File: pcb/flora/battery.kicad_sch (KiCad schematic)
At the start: 38 parts, among them IC3 TP4056X, IC4 FS8205A, IC5 DW01+G, IC6 TPS54302DDCR, IC7 AMS1117-3.3

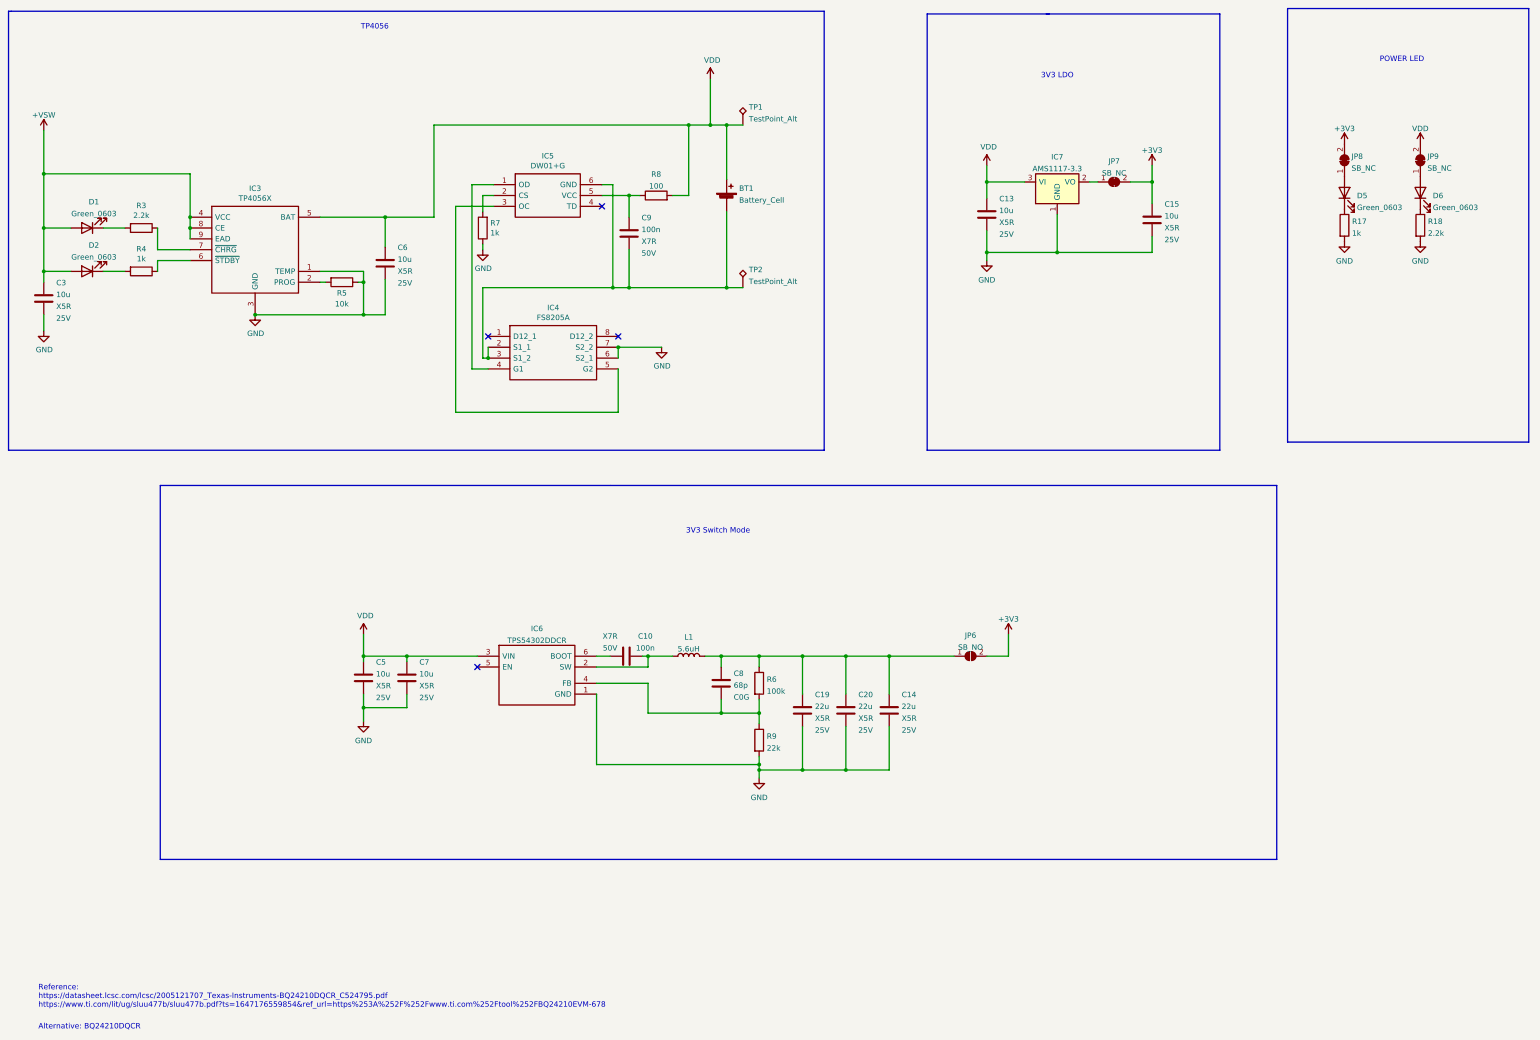
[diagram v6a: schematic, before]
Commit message: Finished schematic for RA-01 design
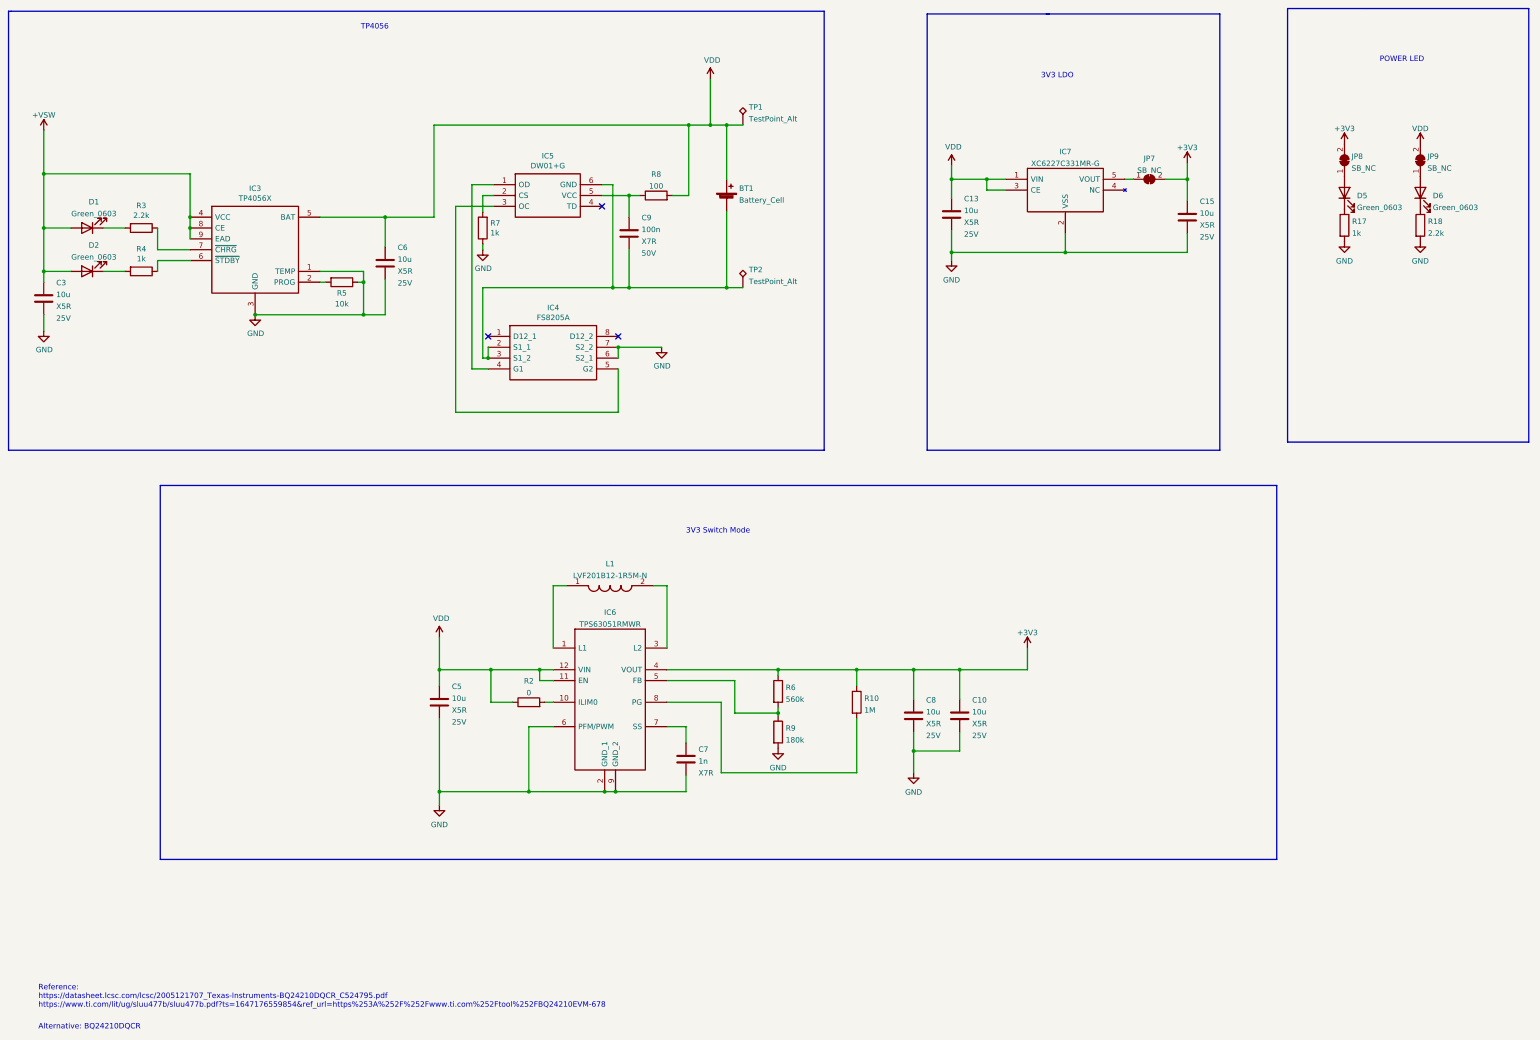
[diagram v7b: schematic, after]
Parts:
- removed C10: 100n, Capacitor_SMD:C_0402_1005Metric, symbol Capacitor_JLC:100n
- removed C14, C19, C20: 22u, Capacitor_SMD:C_0805_2012Metric, symbol Capacitor_JLC:22u
- removed C7: 10u, Capacitor_SMD:C_0805_2012Metric, symbol Capacitor_JLC:10u
- removed C8: 68p, Capacitor_SMD:C_0402_1005Metric, symbol Capacitor_JLC:68p
- removed IC6: TPS54302DDCR, SOT95P280X110-6N, symbol Power-Drivers_JLC:TPS54302DDCR
- removed IC7: AMS1117-3.3, Package_TO_SOT_SMD:SOT-223-3_TabPin2, symbol Power-Drivers_JLC:AMS1117-3.3
- removed JP6: SB_NO, Jumper:SolderJumper-2_P1.3mm_Open_TrianglePad1.0x1.5mm, symbol personal:SB_NO
- removed L1: 5.6uH, SamacSys_Parts:INDPM4040X300N, symbol Inductor_JLC:5.6uH
- removed R6: 100k, Resistor_SMD:R_0402_1005Metric, symbol Resistor_JLC:100k
- removed R9: 22k, Resistor_SMD:R_0402_1005Metric, symbol Resistor_JLC:22k
- added C10, C8: 10u, Capacitor_SMD:C_0805_2012Metric, symbol Capacitor_JLC:10u
- added C7: 1n, Capacitor_SMD:C_0402_1005Metric, symbol Capacitor_JLC:1n
- added IC6: TPS63051RMWR, QFN50P250X250X100-12N-D, symbol Power-Drivers_JLC:TPS63051RMWR
- added IC7: XC6227C331MR-G, SOT95P280X130-5N, symbol Power-Drivers_JLC:XC6227C331MR-G
- added L1: LVF201B12-1R5M-N, LVF201B121R5MN, symbol Inductor_JLC:LVF201B12-1R5M-N
- added R10: 1M, Resistor_SMD:R_0402_1005Metric, symbol Resistor_JLC:1M
- added R2: 0, Resistor_SMD:R_0805_2012Metric_Pad1.20x1.40mm_HandSolder, symbol Resistor_JLC:0
- added R6: 560k, Resistor_SMD:R_0603_1608Metric, symbol Resistor_JLC:560k
- added R9: 180k, Resistor_SMD:R_0402_1005Metric, symbol Resistor_JLC:180k
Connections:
- net +3V3: now also C10.1, C8.1, IC6.4 (VOUT), R10.1, R6.1
- net GND: now also C10.2, C7.2, C8.2, IC6.2 (GND_1), IC6.6 (PFM/PWM), IC6.9 (GND_2), IC7.2 (VSS), R9.2
- net VDD: now also IC6.11 (EN), IC6.12 (VIN), IC7.1 (VIN), IC7.3 (CE), R2.1
- net at JP7.1 (A): now also IC7.5 (VOUT)
- new net: IC6.5 (FB), R6.2, R9.1
- new net: C7.1, IC6.7 (SS)
- new net: IC6.10 (ILIM0), R2.2
- new net: IC6.1 (L1), L1.1
- new net: IC6.3 (L2), L1.2
- new net: IC6.8 (PG), R10.2
- no-connect marks 4 -> 3
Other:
- title: FLORA -> FLORA-RA01H
- moved on the sheet: C13, C15, JP7

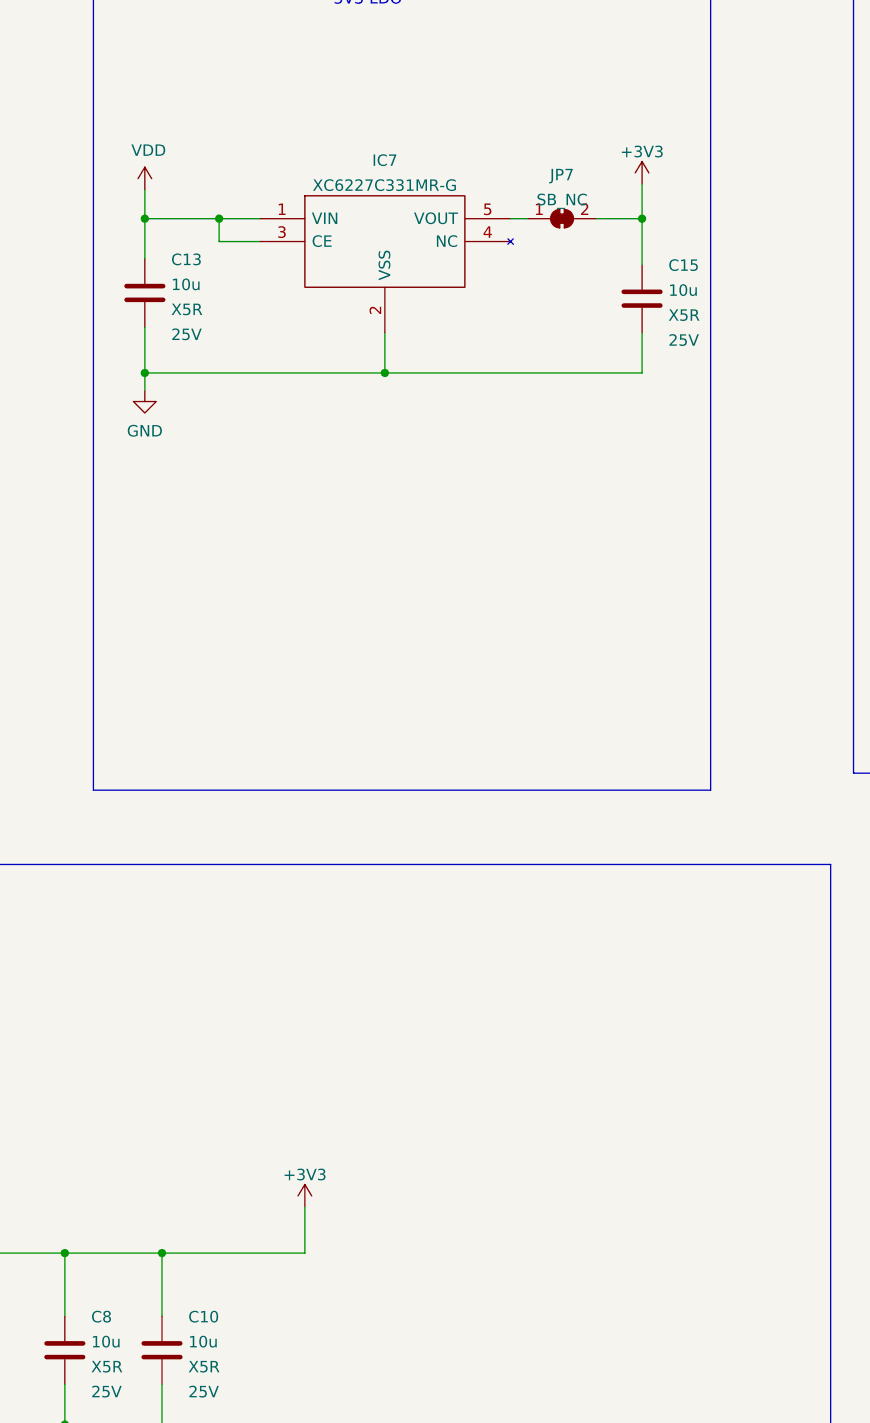
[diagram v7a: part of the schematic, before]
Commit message: base placement completed
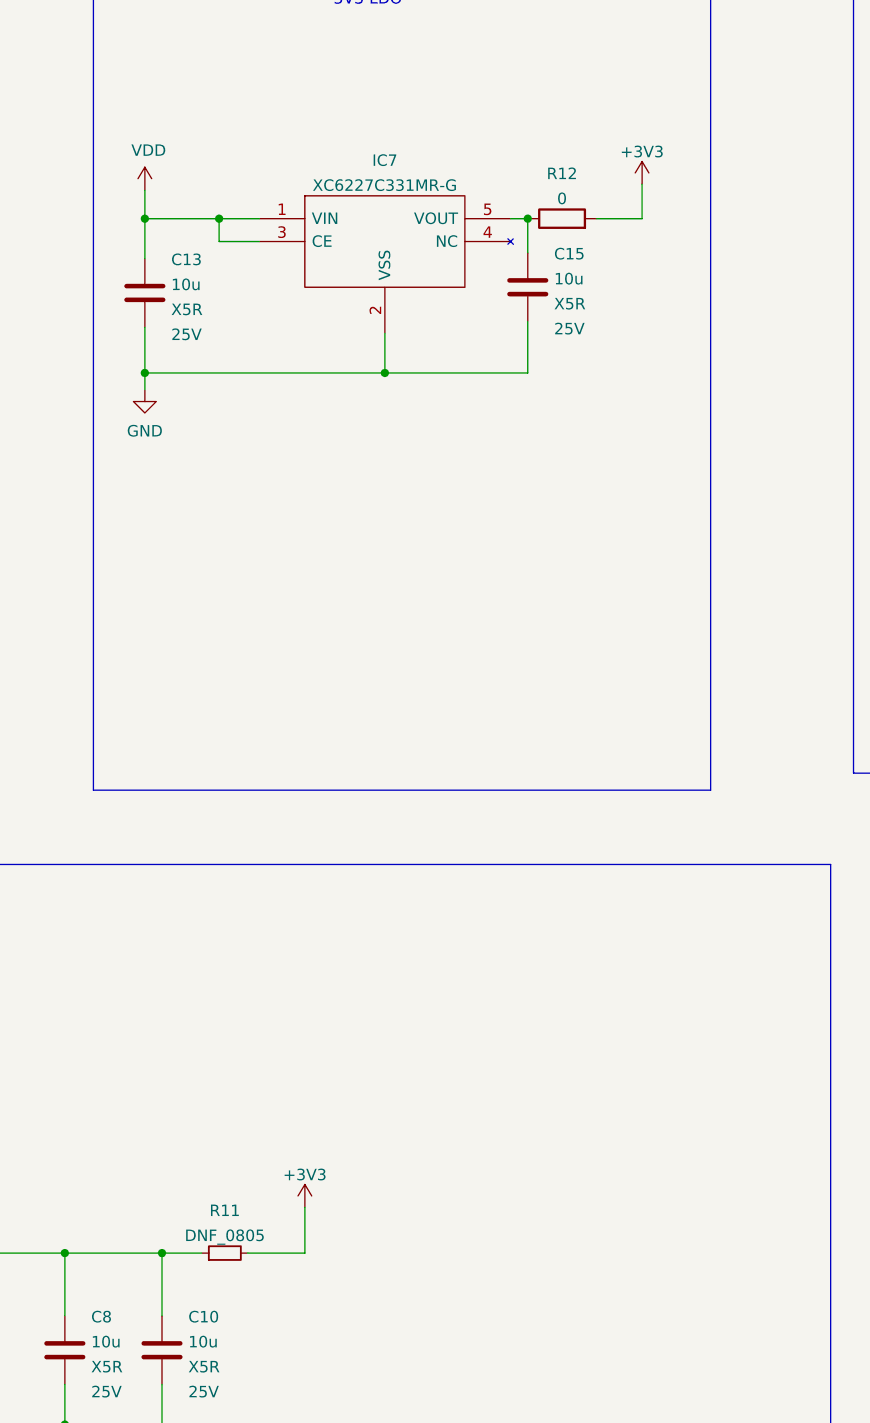
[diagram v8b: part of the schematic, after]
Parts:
- removed JP7: SB_NC, Jumper:SolderJumper-2_P1.3mm_Bridged_Pad1.0x1.5mm, symbol personal:SB_NC
- added R11: DNF_0805, Resistor_SMD:R_0805_2012Metric_Pad1.20x1.40mm_HandSolder, symbol personal:DNF_0805
- added R12: 0, Resistor_SMD:R_0805_2012Metric_Pad1.20x1.40mm_HandSolder, symbol Resistor_JLC:0
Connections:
- net +3V3: now also R11.2, R12.2; no longer C10.1, C15.1, C8.1, IC6.4 (VOUT), R10.1, R6.1
- net at IC7.5 (VOUT): now also C15.1, R12.1
- new net: C10.1, C8.1, IC6.4 (VOUT), R10.1, R11.1, R6.1
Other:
- moved on the sheet: C15
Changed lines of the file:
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@@
   (junction (at 256.54 204.47) (diameter 0) (color 0 0 0 0)
   )
-  (junction (at 320.675 70.485) (diameter 0) (color 0 0 0 0)
-  )
   (junction (at 265.43 87.63) (diameter 0) (color 0 0 0 0)
   )
+  (junction (at 307.975 70.485) (diameter 0) (color 0 0 0 0)
+  )
   (junction (at 127.635 102.235) (diameter 0) (color 0 0 0 0)
   )
@@
   (junction (at 212.725 95.885) (diameter 0) (color 0 0 0 0)
   )
+  (junction (at 157.48 185.42) (diameter 0) (color 0 0 0 0)
+  )
+  (junction (at 208.915 57.785) (diameter 0) (color 0 0 0 0)
+  )
+  (junction (at 102.235 102.235) (diameter 0) (color 0 0 0 0)
+  )
+  (junction (at 273.685 70.485) (diameter 0) (color 0 0 0 0)
+  )
   (junction (at 267.335 185.42) (diameter 0) (color 0 0 0 0)
-  )
-  (junction (at 157.48 185.42) (diameter 0) (color 0 0 0 0)
-  )
-  (junction (at 208.915 57.785) (diameter 0) (color 0 0 0 0)
-  )
-  (junction (at 102.235 102.235) (diameter 0) (color 0 0 0 0)
-  )
-  (junction (at 273.685 70.485) (diameter 0) (color 0 0 0 0)
   )
   (junction (at 86.995 81.915) (diameter 0) (color 0 0 0 0)
@@
     (stroke (width 0) (type default) (color 0 0 0 0))
   )
+  (wire (pts (xy 307.975 81.915) (xy 307.975 87.63))
+    (stroke (width 0) (type default) (color 0 0 0 0))
+  )
   (wire (pts (xy 187.325 109.855) (xy 187.325 112.395))
     (stroke (width 0) (type default) (color 0 0 0 0))
   )
+  (wire (pts (xy 208.915 57.785) (xy 212.725 57.785))
+    (stroke (width 0) (type default) (color 0 0 0 0))
+  )
+  (wire (pts (xy 117.475 94.615) (xy 118.745 94.615))
+    (stroke (width 0) (type default) (color 0 0 0 0))
+  )
   (wire (pts (xy 315.595 70.485) (xy 320.675 70.485))
     (stroke (width 0) (type default) (color 0 0 0 0))
   )
-  (wire (pts (xy 208.915 57.785) (xy 212.725 57.785))
-    (stroke (width 0) (type default) (color 0 0 0 0))
-  )
-  (wire (pts (xy 117.475 94.615) (xy 118.745 94.615))
-    (stroke (width 0) (type default) (color 0 0 0 0))
-  )
   (wire (pts (xy 224.79 194.31) (xy 224.79 195.58))
     (stroke (width 0) (type default) (color 0 0 0 0))
@@
     (stroke (width 0) (type default) (color 0 0 0 0))
   )
-  (wire (pts (xy 320.675 70.485) (xy 320.675 75.565))
-    (stroke (width 0) (type default) (color 0 0 0 0))
-  )
   (wire (pts (xy 265.43 82.55) (xy 265.43 87.63))
     (stroke (width 0) (type default) (color 0 0 0 0))
@@
     (stroke (width 0) (type default) (color 0 0 0 0))
   )
+  (wire (pts (xy 276.86 185.42) (xy 283.21 185.42))
+    (stroke (width 0) (type default) (color 0 0 0 0))
+  )
+  (wire (pts (xy 267.335 185.42) (xy 271.78 185.42))
+    (stroke (width 0) (type default) (color 0 0 0 0))
+  )
   (polyline (pts (xy 80.01 229.87) (xy 80.01 142.24))
     (stroke (width 0) (type default) (color 0 0 0 0))
@@
     (stroke (width 0) (type default) (color 0 0 0 0))
   )
-  (wire (pts (xy 292.1 87.63) (xy 320.675 87.63))
+  (wire (pts (xy 292.1 87.63) (xy 307.975 87.63))
     (stroke (width 0) (type default) (color 0 0 0 0))
   )
@@
     (stroke (width 0) (type default) (color 0 0 0 0))
   )
-  (wire (pts (xy 320.675 87.63) (xy 320.675 83.185))
-    (stroke (width 0) (type default) (color 0 0 0 0))
-  )
   (polyline (pts (xy 259.715 133.985) (xy 259.715 31.75))
     (stroke (width 0) (type default) (color 0 0 0 0))
@@
     (stroke (width 0) (type default) (color 0 0 0 0))
   )
+  (wire (pts (xy 307.975 70.485) (xy 307.975 74.295))
+    (stroke (width 0) (type default) (color 0 0 0 0))
+  )
   (wire (pts (xy 183.515 74.295) (xy 189.865 74.295))
     (stroke (width 0) (type default) (color 0 0 0 0))
@@
   )
   (wire (pts (xy 203.835 57.785) (xy 208.915 57.785))
-    (stroke (width 0) (type default) (color 0 0 0 0))
-  )
-  (wire (pts (xy 267.335 185.42) (xy 283.21 185.42))
     (stroke (width 0) (type default) (color 0 0 0 0))
   )
@@
     (pin "1")
   )
-  (symbol (lib_id "personal:SB_NC") (at 311.785 70.485 0) (unit 1)
-    (in_bom yes) (on_board yes) (fields_autoplaced)
-    (property "Reference" "JP7" (id 0) (at 311.785 65.6295 0))
-    (property "Value" "SB_NC" (id 1) (at 311.785 68.4046 0))
-    (property "Footprint" "Jumper:SolderJumper-2_P1.3mm_Bridged_Pad1.0x1.5mm" (id 2) (at 311.785 70.485 0)
+  (symbol (lib_id "Resistor_JLC:0") (at 311.785 70.485 90) (unit 1)
+    (in_bom yes) (on_board yes) (fields_autoplaced)
+    (property "Reference" "R12" (id 0) (at 311.785 65.5025 90))
+    (property "Value" "0" (id 1) (at 311.785 68.2776 90))
+    (property "Footprint" "Resistor_SMD:R_0805_2012Metric_Pad1.20x1.40mm_HandSolder" (id 2) (at 311.785 72.263 90)
       (effects (font (size 1.27 1.27)) hide)
     )
     (property "Datasheet" "~" (id 3) (at 311.785 70.485 0)
+      (effects (font (size 1.27 1.27)) hide)
+    )
+    (property "LCSC" "C17477" (id 4) (at 311.785 70.485 0)
       (effects (font (size 1.27 1.27)) hide)
     )
@@
     (pin "8")
   )
-  (symbol (lib_id "Capacitor_JLC:10u") (at 320.675 79.375 0) (unit 1)
-    (in_bom yes) (on_board yes) (fields_autoplaced)
-    (property "Reference" "C15" (id 0) (at 323.596 75.6914 0)
-      (effects (font (size 1.27 1.27)) (justify left))
-    )
-    (property "Value" "10u" (id 1) (at 323.596 78.4665 0)
-      (effects (font (size 1.27 1.27)) (justify left))
-    )
-    (property "Footprint" "Capacitor_SMD:C_0805_2012Metric" (id 2) (at 321.6402 83.185 0)
-      (effects (font (size 1.27 1.27)) hide)
-    )
-    (property "Datasheet" "~" (id 3) (at 320.675 79.375 0)
-      (effects (font (size 1.27 1.27)) hide)
-    )
-    (property "Type" "X5R" (id 4) (at 323.596 81.2416 0)
-      (effects (font (size 1.27 1.27)) (justify left))
-    )
-    (property "LCSC" "C15850" (id 5) (at 320.675 79.375 0)
-      (effects (font (size 1.27 1.27)) hide)
-    )
-    (property "Voltage" "25V" (id 6) (at 323.596 84.0167 0)
+  (symbol (lib_id "Capacitor_JLC:10u") (at 307.975 78.105 0) (unit 1)
+    (in_bom yes) (on_board yes) (fields_autoplaced)
+    (property "Reference" "C15" (id 0) (at 310.896 74.4214 0)
+      (effects (font (size 1.27 1.27)) (justify left))
+    )
+    (property "Value" "10u" (id 1) (at 310.896 77.1965 0)
+      (effects (font (size 1.27 1.27)) (justify left))
+    )
+    (property "Footprint" "Capacitor_SMD:C_0805_2012Metric" (id 2) (at 308.9402 81.915 0)
+      (effects (font (size 1.27 1.27)) hide)
+    )
+    (property "Datasheet" "~" (id 3) (at 307.975 78.105 0)
+      (effects (font (size 1.27 1.27)) hide)
+    )
+    (property "Type" "X5R" (id 4) (at 310.896 79.9716 0)
+      (effects (font (size 1.27 1.27)) (justify left))
+    )
+    (property "LCSC" "C15850" (id 5) (at 307.975 78.105 0)
+      (effects (font (size 1.27 1.27)) hide)
+    )
+    (property "Voltage" "25V" (id 6) (at 310.896 82.7467 0)
       (effects (font (size 1.27 1.27)) (justify left))
     )
@@
       (effects (font (size 1.27 1.27)) hide)
     )
+    (pin "1")
+    (pin "2")
+  )
+  (symbol (lib_id "personal:DNF_0805") (at 274.32 185.42 90) (unit 1)
+    (in_bom yes) (on_board yes) (fields_autoplaced)
+    (property "Reference" "R11" (id 0) (at 274.32 180.7169 90))
+    (property "Value" "DNF_0805" (id 1) (at 274.32 183.492 90))
+    (property "Footprint" "Resistor_SMD:R_0805_2012Metric_Pad1.20x1.40mm_HandSolder" (id 2) (at 274.32 185.42 0)
+      (effects (font (size 1.27 1.27)) hide)
+    )
+    (property "Datasheet" "~" (id 3) (at 274.32 185.42 0)
+      (effects (font (size 1.27 1.27)) hide)
+    )
